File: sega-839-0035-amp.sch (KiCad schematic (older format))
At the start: 60 parts, among them IC1 MB3733, IC2 MB3733, IC4 MB3110A, IC5 MB3110A, J1 4-pin Molex, J2 6-Pin Molex, J3 8-Pin Molex, Q101 2SC458, Q2 Q_NPN_ECB, Q201 2SC458

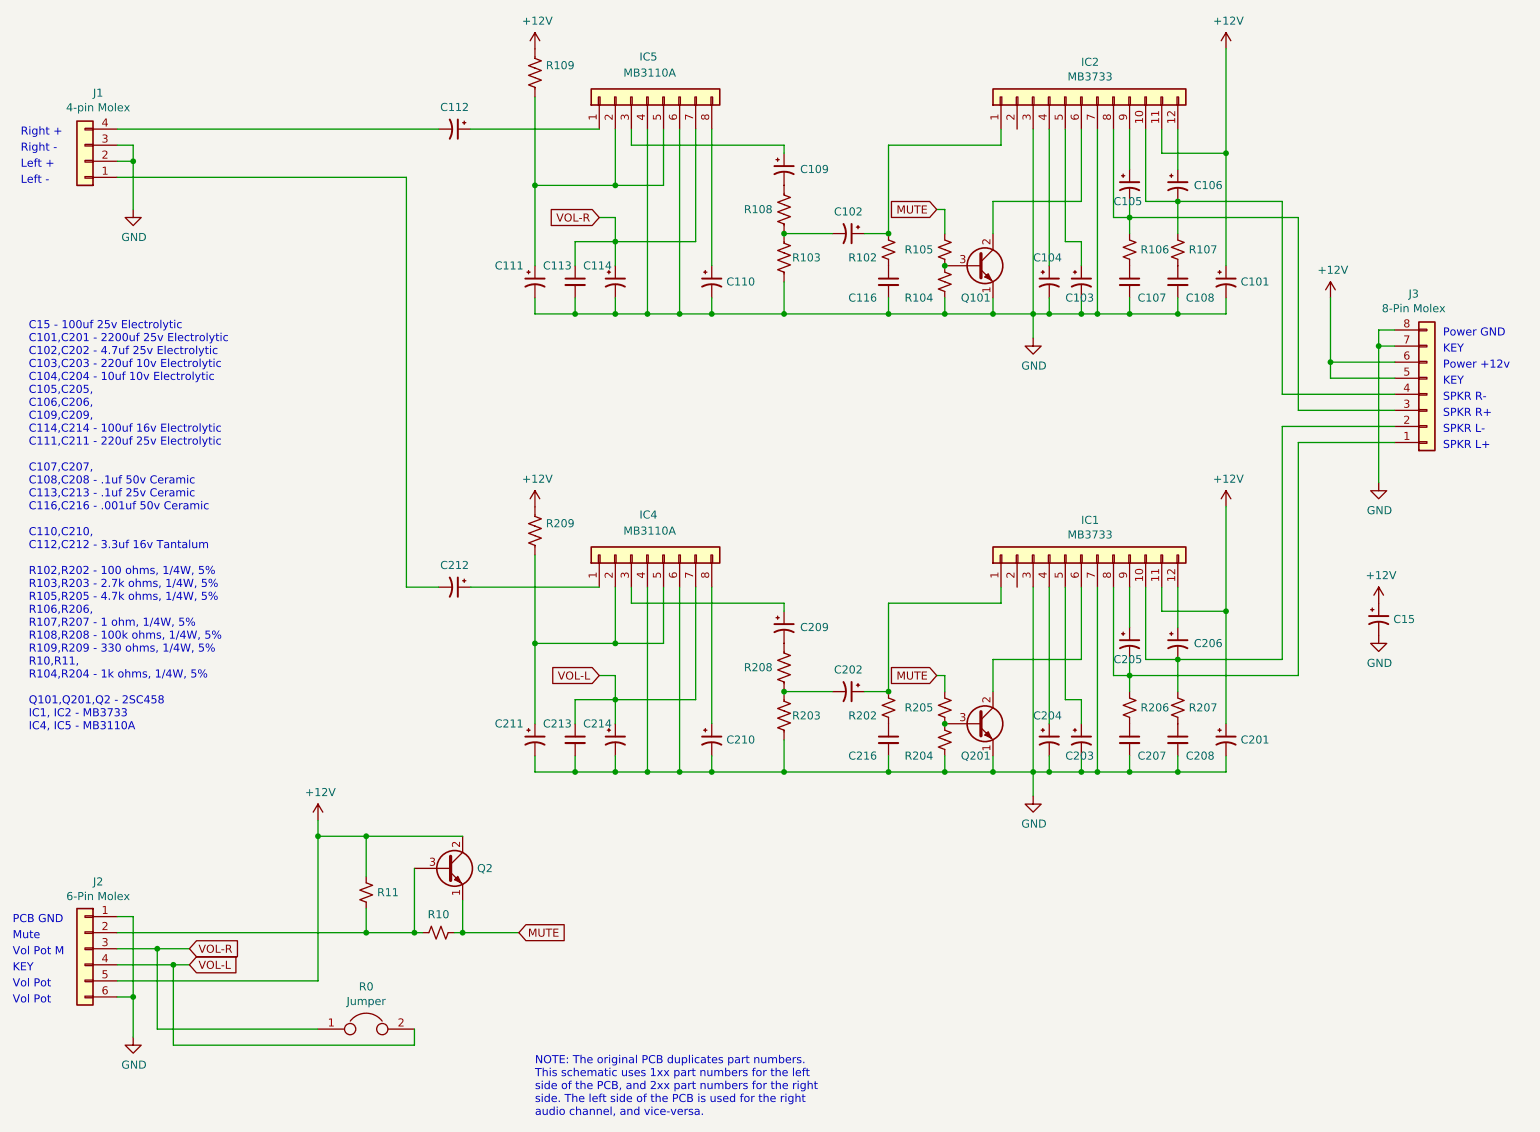
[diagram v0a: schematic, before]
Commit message: swapped C3/C4, fixed voltage ratings
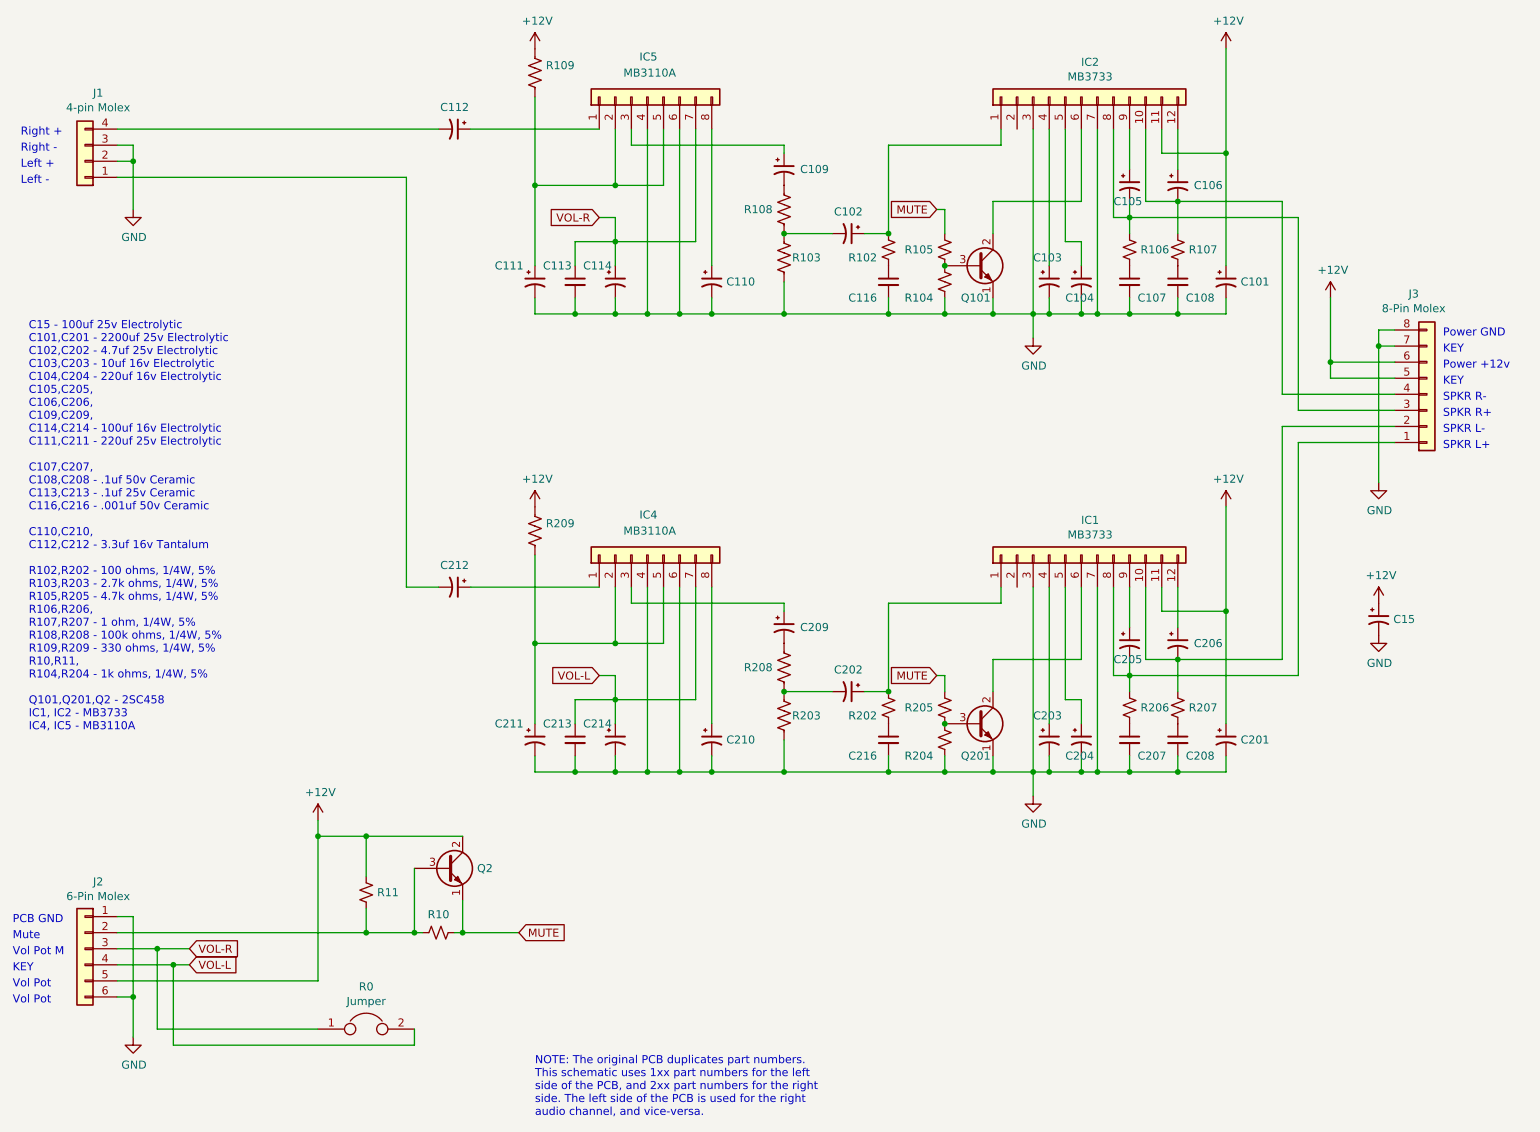
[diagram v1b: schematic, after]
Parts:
- renumbered C104 to C103, C103 to C104, C204 to C203, C203 to C204
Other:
- note added: "C15 - 100uf 25v Electrolytic\nC101,C201 - 2200uf 25v Electrolytic\nC102,C202 - 4.7uf 25v Electrolytic\nC103,C203 - 10uf 16v Electrolytic\nC104,C204 - 220uf 16v Electrolytic\nC105,C205,\nC106,C206,\nC109,C209,\nC114,C214 - 100uf 16v Electrolytic\nC111,C211 - 220uf 25v Electrolytic\n\nC107,C207,\nC108,C208 - .1uf 50v Ceramic\nC113,C213 - .1uf 25v Ceramic\nC116,C216 - .001uf 50v Ceramic\n\nC110,C210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"
- note removed: "C15 - 100uf 25v Electrolytic\nC101,C201 - 2200uf 25v Electrolytic\nC102,C202 - 4.7uf 25v Electrolytic\nC103,C203 - 220uf 10v Electrolytic\nC104,C204 - 10uf 10v Electrolytic\nC105,C205,\nC106,C206,\nC109,C209,\nC114,C214 - 100uf 16v Electrolytic\nC111,C211 - 220uf 25v Electrolytic\n\nC107,C207,\nC108,C208 - .1uf 50v Ceramic\nC113,C213 - .1uf 25v Ceramic\nC116,C216 - .001uf 50v Ceramic\n\nC110,C210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"
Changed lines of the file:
@@
 Sheet 1 1
 Title "Sega 839-0035 Amplifier"
-Date "2022-07-17"
-Rev "1.0"
+Date "2022-07-19"
+Rev "1.1"
 Comp "Marc Deslauriers"
 Comment1 ""
@@
 $EndComp
 $Comp
-L Device:CP1_Small C104
+L Device:CP1_Small C103
 U 1 1 62D4C99C
 P 7300 2550
-F 0 "C104" H 7200 2700 50  0000 L CNN
+F 0 "C103" H 7200 2700 50  0000 L CNN
 F 1 "CP1_Small" H 7391 2505 50  0001 L CNN
 F 2 "" H 7300 2550 50  0001 C CNN
@@
 $EndComp
 $Comp
-L Device:CP1_Small C103
+L Device:CP1_Small C104
 U 1 1 62D4CE13
 P 7500 2550
-F 0 "C103" H 7400 2450 50  0000 L CNN
+F 0 "C104" H 7400 2450 50  0000 L CNN
 F 1 "CP1_Small" H 7591 2505 50  0001 L CNN
 F 2 "" H 7500 2550 50  0001 C CNN
@@
 $EndComp
 $Comp
-L Device:CP1_Small C204
+L Device:CP1_Small C203
 U 1 1 62F1FC8B
 P 7300 5400
-F 0 "C204" H 7200 5550 50  0000 L CNN
+F 0 "C203" H 7200 5550 50  0000 L CNN
 F 1 "CP1_Small" H 7391 5355 50  0001 L CNN
 F 2 "" H 7300 5400 50  0001 C CNN
@@
 $EndComp
 $Comp
-L Device:CP1_Small C203
+L Device:CP1_Small C204
 U 1 1 62F1FC91
 P 7500 5400
-F 0 "C203" H 7400 5300 50  0000 L CNN
+F 0 "C204" H 7400 5300 50  0000 L CNN
 F 1 "CP1_Small" H 7591 5355 50  0001 L CNN
 F 2 "" H 7500 5400 50  0001 C CNN
@@
 $EndComp
 Text Notes 950  5350 0    50   ~ 0
-C15 - 100uf 25v Electrolytic\nC101,C201 - 2200uf 25v Electrolytic\nC102,C202 - 4.7uf 25v Electrolytic\nC103,C203 - 220uf 10v Electrolytic\nC104,C204 - 10uf 10v Electrolytic\nC105,C205,\nC106,C206,\nC109,C209,\nC114,C214 - 100uf 16v Electrolytic\nC111,C211 - 220uf 25v Electrolytic\n\nC107,C207,\nC108,C208 - .1uf 50v Ceramic\nC113,C213 - .1uf 25v Ceramic\nC116,C216 - .001uf 50v Ceramic\n\nC110,C210,\nC112,C212 - 3.3uf 16v Tantalum\n\nR102,R202 - 100 ohms, 1/4W, 5%\nR103,R203 - 2.7k ohms, 1/4W, 5%\nR105,R205 - 4.7k ohms, 1/4W, 5%\nR106,R206,\nR107,R207 - 1 ohm, 1/4W, 5%\nR108,R208 - 100k ohms, 1/4W, 5%\nR109,R209 - 330 ohms, 1/4W, 5%\nR10,R11,\nR104,R204 - 1k ohms, 1/4W, 5%\n\nQ101,Q201,Q2 - 2SC458\nIC1, IC2 - MB3733\nIC4, IC5 - MB3110A
+C15 - 100uf 25v Electrolytic\nC101,C201 - 2200uf 25v Electrolytic\nC102,C202 - 4.7uf 25v Electrolytic\nC103,C203 - 10uf 16v Electrolytic\nC104,C204 - 220uf 16v Electrolytic\nC105,C205,\nC106,C206,\nC109,C209,\nC114,C214 - 100uf 16v Electrolytic\nC111,C211 - 220uf 25v Electrolytic\n\nC107,C207,\nC108,C208 - .1uf 50v Ceramic\nC113,C213 - .1uf 25v Ceramic\nC116,C216 - .001uf 50v Ceramic\n\nC110,C210,\nC112,C212 - 3.3uf 16v Tantalum\n\nR102,R202 - 100 ohms, 1/4W, 5%\nR103,R203 - 2.7k ohms, 1/4W, 5%\nR105,R205 - 4.7k ohms, 1/4W, 5%\nR106,R206,\nR107,R207 - 1 ohm, 1/4W, 5%\nR108,R208 - 100k ohms, 1/4W, 5%\nR109,R209 - 330 ohms, 1/4W, 5%\nR10,R11,\nR104,R204 - 1k ohms, 1/4W, 5%\n\nQ101,Q201,Q2 - 2SC458\nIC1, IC2 - MB3733\nIC4, IC5 - MB3110A
 $EndSCHEMATC
